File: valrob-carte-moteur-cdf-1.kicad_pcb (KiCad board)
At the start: 2 copper layers, 63 x 50 mm, 85 parts, among them J1 USB_C_Receptacle_USB2.0_14P, J2 Conn_01x02, J3 Conn_01x02, J4 Conn_01x04_Pin, J5 Conn_01x08, J6 Conn_01x02, J7 Conn_01x02, J8 Conn_01x08, SW1 SW_Push, SW2 SW_Push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

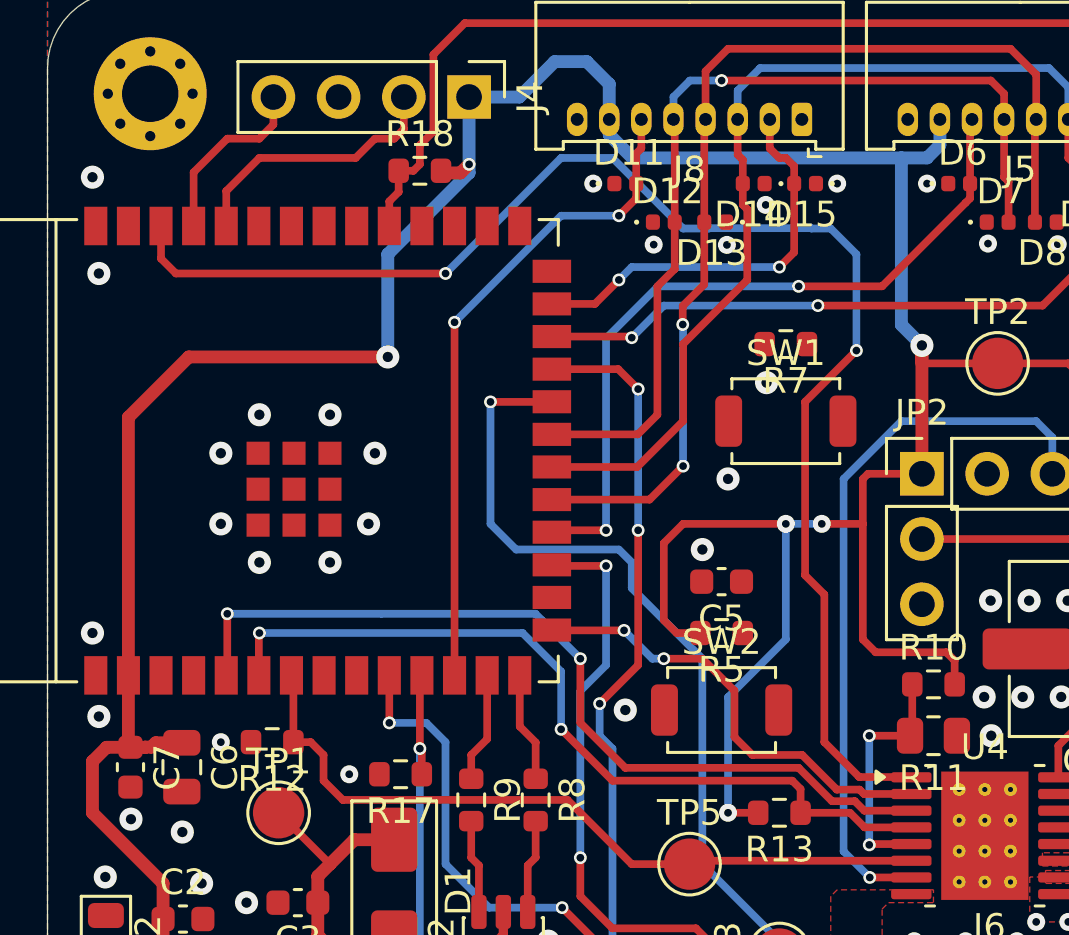
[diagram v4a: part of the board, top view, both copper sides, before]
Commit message: pcb: add CHIP_PU AND BOOT routing
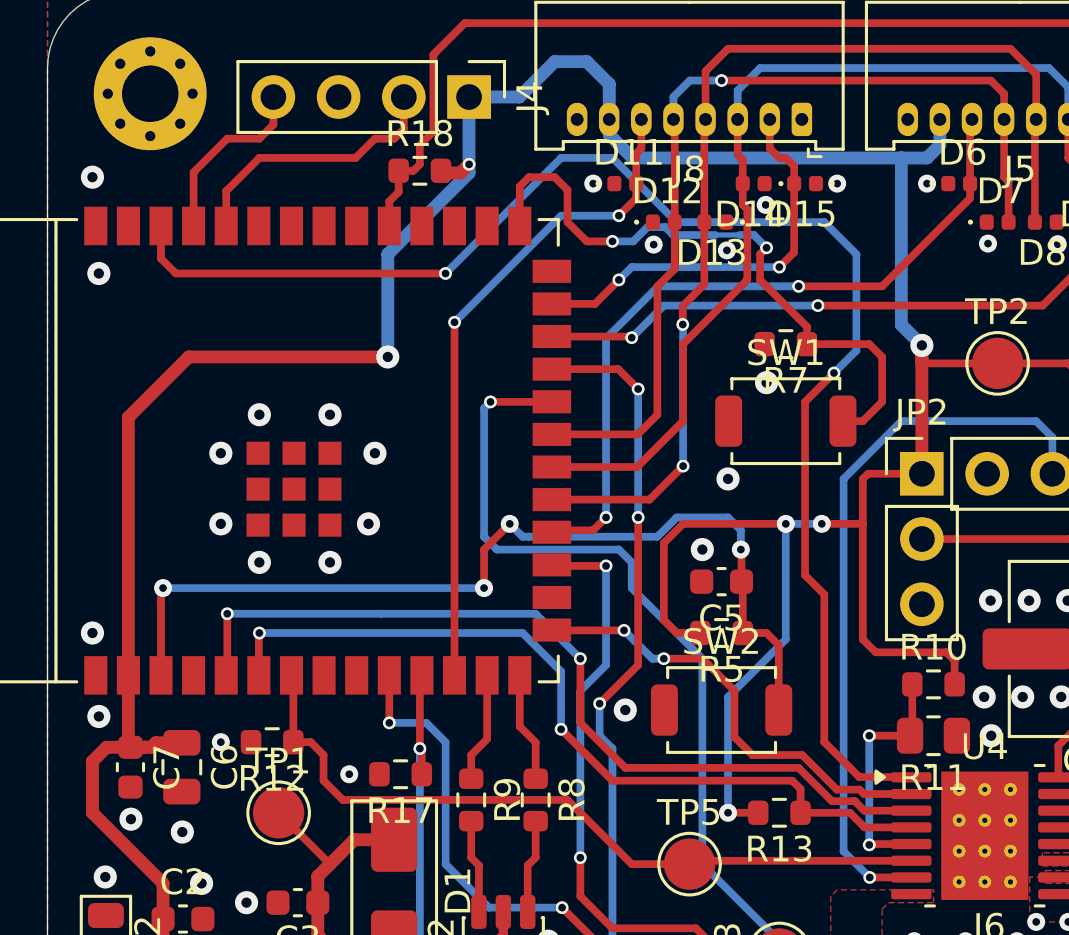
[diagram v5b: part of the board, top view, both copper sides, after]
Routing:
- net /CHIP_PU: track 0.00 -> 36.7 mm, vias 0 -> 4
- net /BOOT: track 0.00 -> 25.0 mm, vias 0 -> 2
- net /DC Driver 2/EN/IN1: track 54.8 -> 55.5 mm
